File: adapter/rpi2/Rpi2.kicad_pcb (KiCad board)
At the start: 2 copper layers, 56.5 x 65.4 mm, 4 parts

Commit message: routing all traces on pcb
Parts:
- moved Display1 13.7 mm to (150.4, 126.4)
- moved Display2 13.7 mm to (136.4, 126.4)
- moved RPi2 13.2 mm to (105.0, 157.0)
- moved SNES1 8.50 mm to (150.4, 144.7)
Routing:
- net /OE: track 0.00 -> 128.1 mm
- net CLK: track 0.00 -> 127.2 mm
- net STB: track 0.00 -> 125.8 mm
- net SNES_LATCH: track 0.00 -> 105.2 mm
- net SNES_CLK: track 0.00 -> 102.8 mm
- net C: track 0.00 -> 84.2 mm
- net 3V3: track 0.00 -> 82.7 mm
- net A: track 0.00 -> 81.1 mm
- net D: track 0.00 -> 72.6 mm
- net B: track 0.00 -> 70.6 mm, vias 0 -> 2
- net [1]B0: track 0.00 -> 65.8 mm
- net [1]R1: track 0.00 -> 62.4 mm
- net [1]R0: track 0.00 -> 57.7 mm
- net [1]B1: track 0.00 -> 53.3 mm
- net [1]G0: track 0.00 -> 50.5 mm
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- added copper zone on F.Cu, net GND
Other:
- board size 56.5 x 65.4 mm -> 56 x 65 mm
- net class Default: clearance 0.2 -> 0.1; trace_width 0.25 -> 0.2
- net class power added: clearance 0.1, trace_width 0.25, via_dia 0.6, via_drill 0.4
- rule trace_clearance: 0.2 -> 0.1
- rule trace_min: 0.2 -> 0.1

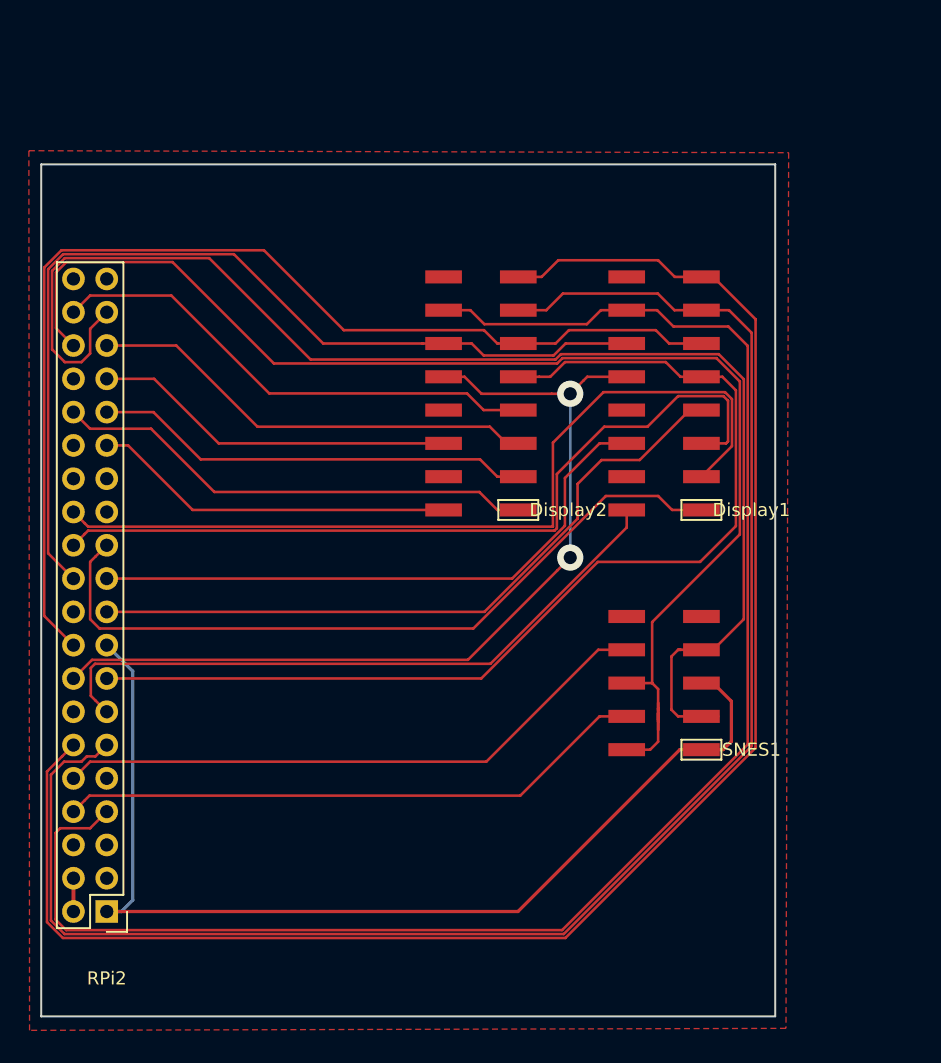
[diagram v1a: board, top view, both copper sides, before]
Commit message: adding PCF8574, finished routing, drill holes unsuitable
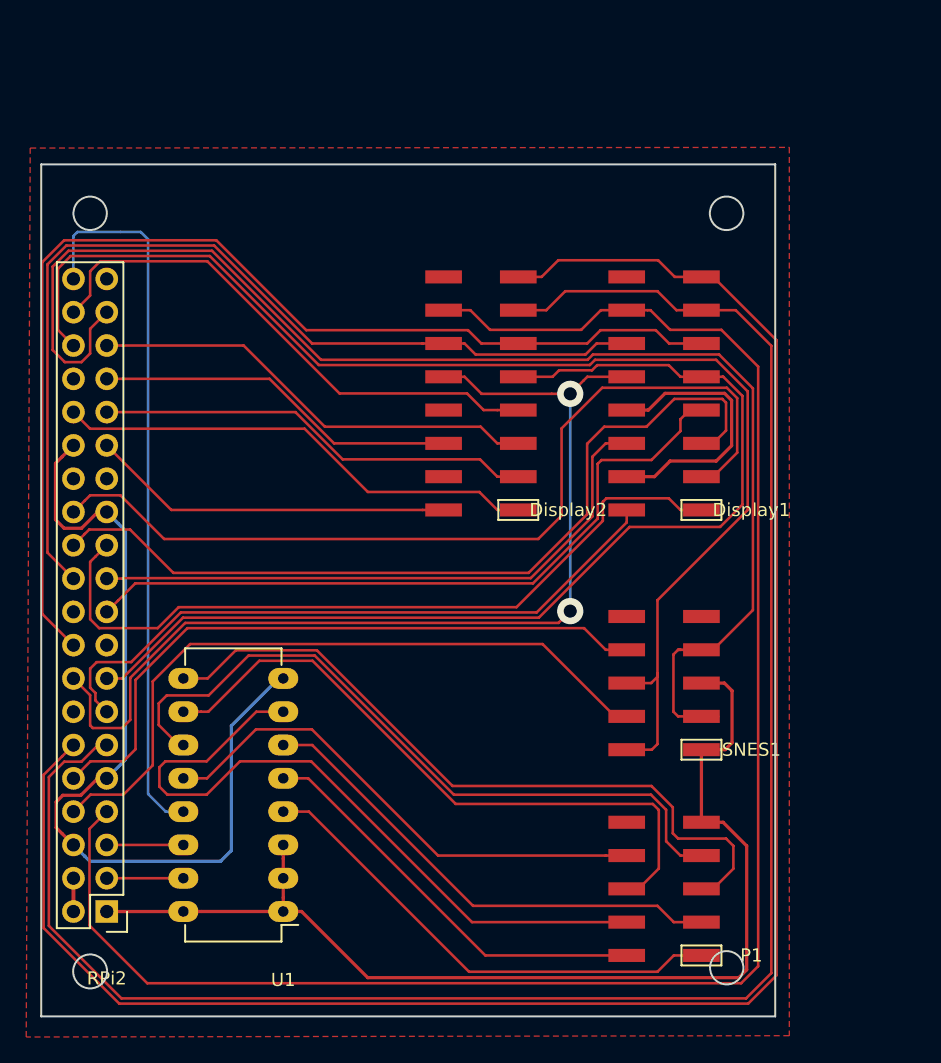
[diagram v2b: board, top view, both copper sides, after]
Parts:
- added P1: CONN_02X05, Pin_Headers_SMD:Pin_Header_SMD_02x05, F.Cu at (150.4, 160.4)
- added U1: PCF8574, Housings_DIP:DIP-16_W7.62mm_LongPads, F.Cu at (118.5, 157.0)
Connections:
- RPi2 pad 14: GND -> Net-(RPi2-Pad14)
- RPi2 pad 17: 3V3 -> Net-(RPi2-Pad17)
- RPi2 pad 20: GND -> Net-(RPi2-Pad20)
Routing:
- net GND: track 0.22 -> 90.2 mm
- net Net-(P1-Pad5): track 0.00 -> 55.0 mm
- net Net-(RPi2-Pad40): track 0.00 -> 54.9 mm
- net Net-(P1-Pad7): track 0.00 -> 54.8 mm
- net Net-(P1-Pad4): track 0.00 -> 54.7 mm
- net Net-(P1-Pad6): track 0.00 -> 50.2 mm
- net Net-(P1-Pad8): track 0.00 -> 39.4 mm
- net Net-(P1-Pad3): track 0.00 -> 37.5 mm
- net Net-(P1-Pad1): track 0.00 -> 37.5 mm
- net Net-(P1-Pad2): track 0.00 -> 31.8 mm
- net CLK: track 127.2 -> 144.5 mm
- net /OE: track 128.1 -> 145.3 mm
- net STB: track 125.8 -> 135.4 mm
- net B: track 70.6 -> 79.4 mm
- net SNES_DATA0: track 45.2 -> 53.5 mm
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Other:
- outline, holes or cut-outs redrawn
- net class Default: clearance 0.1 -> 0.2
- net class power: clearance 0.1 -> 0.2
- rule trace_clearance: 0.1 -> 0.2

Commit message: finalized board
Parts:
- added REF**: Symbol_OSHW-Logo_CopperTop, Symbols:Symbol_OSHW-Logo_CopperTop, F.Cu at (143.8, 155.7)
- moved P1 17.6 mm to (136.4, 149.7)
- moved U1 0.91 mm to (119.4, 157.0)
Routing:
- net Net-(P1-Pad6): track 50.2 -> 26.4 mm
- net Net-(P1-Pad2): track 31.8 -> 12.5 mm
- net Net-(P1-Pad3): track 37.5 -> 18.2 mm
- net Net-(P1-Pad5): track 55.0 -> 35.7 mm
- net Net-(P1-Pad4): track 54.7 -> 35.6 mm
- net Net-(P1-Pad1): track 37.5 -> 18.4 mm
- net Net-(P1-Pad7): track 54.8 -> 35.9 mm
- net Net-(P1-Pad8): track 39.4 -> 20.9 mm
- net 3V3: track 84.5 -> 96.3 mm
- net GND: track 90.2 -> 99.5 mm, vias 0 -> 1
- net STB: track 135.4 -> 132.3 mm
- net CLK: track 144.5 -> 147.3 mm
- net /OE: track 145.3 -> 148.0 mm
- net Net-(RPi2-Pad40): track 54.9 -> 53.3 mm, vias 0 -> 1
- net SNES_DATA1: track 50.7 -> 52.1 mm
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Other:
- board size 56 x 65 mm -> 56.8 x 65 mm

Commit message: changed part names
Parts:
- removed P1: CONN_02X05, Pin_Headers_SMD:Pin_Header_SMD_02x05
- added Expander1: CONN_02X05, Pin_Headers_SMD:Pin_Header_SMD_02x05, F.Cu at (136.4, 149.7)
- ?: renamed from REF**; value Symbol_OSHW-Logo_CopperTop -> (none)
- renumbered SNES1 to SNES1+2
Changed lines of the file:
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@@
     (links 66)
     (no_connects 0)
-    (area 98.8568 98.7044 157.619667 166.573201)
+    (area 99.674999 99.924999 156.575001 165.075001)
     (thickness 1.6)
     (drawings 8)
-    (tracks 420)
+    (tracks 419)
     (zones 0)
     (modules 7)
@@
     (descr "16-lead dip package, row spacing 7.62 mm (300 mils), longer pads")
     (tags "dil dip 2.54 300")
-    (fp_text reference U1 (at 0 -5.22 180) (layer F.SilkS)
-      (effects (font (size 1 1) (thickness 0.15)))
-    )
-    (fp_text value PCF8574 (at 0 -3.72 180) (layer F.Fab)
+    (fp_text reference U1 (at 3.7592 -3.937 180) (layer F.SilkS)
+      (effects (font (size 1 1) (thickness 0.15)))
+    )
+    (fp_text value PCF8574 (at 3.7592 21.3106 180) (layer F.Fab)
       (effects (font (size 1 1) (thickness 0.15)))
     )
@@
     )
   )
-  (module Pin_Headers_SMD:Pin_Header_SMD_02x05 (layer F.Cu)
-    (at 136.4084 149.6822 180)
-    (fp_text reference P1 (at -3.81 0 180) (layer F.SilkS)
-      (effects (font (size 1 1) (thickness 0.15)))
-    )
-    (fp_text value CONN_02X05 (at 0 -2.032 180) (layer F.Fab)
-      (effects (font (size 1 1) (thickness 0.15)))
-    )
-    (fp_line (start -1.524 -0.762) (end 1.524 -0.762) (layer F.SilkS) (width 0.15))
-    (fp_line (start 1.524 -0.762) (end 1.524 0.762) (layer F.SilkS) (width 0.15))
-    (fp_line (start 1.524 0.762) (end -1.524 0.762) (layer F.SilkS) (width 0.15))
-    (fp_line (start -1.524 0.762) (end -1.524 -0.762) (layer F.SilkS) (width 0.15))
-    (pad 1 smd rect (at 0 0 180) (size 2.8 1) (layers F.Cu F.Paste F.Mask)
-      (net 32 "Net-(P1-Pad1)"))
-    (pad 2 smd rect (at 5.7 0 180) (size 2.8 1) (layers F.Cu F.Paste F.Mask)
-      (net 33 "Net-(P1-Pad2)"))
-    (pad 3 smd rect (at 0 2.54 180) (size 2.8 1) (layers F.Cu F.Paste F.Mask)
-      (net 34 "Net-(P1-Pad3)"))
-    (pad 4 smd rect (at 5.7 2.54 180) (size 2.8 1) (layers F.Cu F.Paste F.Mask)
-      (net 35 "Net-(P1-Pad4)"))
-    (pad 5 smd rect (at 0 5.08 180) (size 2.8 1) (layers F.Cu F.Paste F.Mask)
-      (net 36 "Net-(P1-Pad5)"))
-    (pad 6 smd rect (at 5.7 5.08 180) (size 2.8 1) (layers F.Cu F.Paste F.Mask)
-      (net 37 "Net-(P1-Pad6)"))
-    (pad 7 smd rect (at 0 7.62 180) (size 2.8 1) (layers F.Cu F.Paste F.Mask)
-      (net 38 "Net-(P1-Pad7)"))
-    (pad 8 smd rect (at 5.7 7.62 180) (size 2.8 1) (layers F.Cu F.Paste F.Mask)
-      (net 39 "Net-(P1-Pad8)"))
-    (pad 9 smd rect (at 0 10.16 180) (size 2.8 1) (layers F.Cu F.Paste F.Mask)
-      (net 21 3V3))
-    (pad 10 smd rect (at 5.7 10.16 180) (size 2.8 1) (layers F.Cu F.Paste F.Mask)
-      (net 4 GND))
-  )
   (module Pin_Headers:Pin_Header_Straight_2x20 (layer F.Cu)
     (at 105 157 180)
     (descr "Through hole pin header")
     (tags "pin header")
-    (fp_text reference RPi2 (at 0 -5.1 180) (layer F.SilkS)
-      (effects (font (size 1 1) (thickness 0.15)))
-    )
-    (fp_text value CONN_02X20 (at 0 -3.1 180) (layer F.Fab)
+    (fp_text reference RPi2 (at 1.2664 -2.6136 180) (layer F.SilkS)
+      (effects (font (size 1 1) (thickness 0.15)))
+    )
+    (fp_text value CONN_02X20 (at -2.7976 44.7828 450) (layer F.Fab)
       (effects (font (size 1 1) (thickness 0.15)))
     )
@@
   (module Pin_Headers_SMD:Pin_Header_SMD_02x08 (layer F.Cu)
     (at 136.398 126.365 180)
-    (fp_text reference Display2 (at -3.81 0 180) (layer F.SilkS)
-      (effects (font (size 1 1) (thickness 0.15)))
-    )
-    (fp_text value CONN_02X08 (at 0 -2.032 180) (layer F.Fab)
+    (fp_text reference Display2 (at 3.0988 -2.0574 180) (layer F.SilkS)
+      (effects (font (size 1 1) (thickness 0.15)))
+    )
+    (fp_text value CONN_02X08 (at 2.7432 20.0406 180) (layer F.Fab)
       (effects (font (size 1 1) (thickness 0.15)))
     )
@@
   (module Pin_Headers_SMD:Pin_Header_SMD_02x05 (layer F.Cu)
     (at 150.368 144.653 180)
-    (fp_text reference SNES1 (at -3.81 0 180) (layer F.SilkS)
-      (effects (font (size 1 1) (thickness 0.15)))
-    )
-    (fp_text value CONN_02X05 (at 0 -2.032 180) (layer F.Fab)
+    (fp_text reference SNES1+2 (at 2.6924 -2.2606 180) (layer F.SilkS)
+      (effects (font (size 1 1) (thickness 0.15)))
+    )
+    (fp_text value CONN_02X05 (at 2.8448 12.4206 180) (layer F.Fab)
       (effects (font (size 1 1) (thickness 0.15)))
     )
@@
   (module Pin_Headers_SMD:Pin_Header_SMD_02x08 (layer F.Cu)
     (at 150.368 126.365 180)
-    (fp_text reference Display1 (at -3.81 0 180) (layer F.SilkS)
-      (effects (font (size 1 1) (thickness 0.15)))
-    )
-    (fp_text value CONN_02X08 (at 0 -2.032 180) (layer F.Fab)
+    (fp_text reference Display1 (at 2.794 -2.3622 180) (layer F.SilkS)
+      (effects (font (size 1 1) (thickness 0.15)))
+    )
+    (fp_text value CONN_02X08 (at 3.0988 19.9898 180) (layer F.Fab)
       (effects (font (size 1 1) (thickness 0.15)))
     )
@@
     (descr "Symbol, OSHW-Logo, Copper Top,")
     (tags "Symbol, OSHW-Logo, Copper Top,")
-    (fp_text reference REF** (at 0.09906 -4.38912) (layer F.SilkS)
-      (effects (font (size 1 1) (thickness 0.15)))
-    )
-    (fp_text value Symbol_OSHW-Logo_CopperTop (at 0.30988 6.56082) (layer F.Fab)
+    (fp_text reference "" (at 0.09906 -4.38912) (layer F.SilkS)
+      (effects (font (size 1 1) (thickness 0.15)))
+    )
+    (fp_text value "" (at -3.2512 1.6256) (layer F.Fab)
       (effects (font (size 1 1) (thickness 0.15)))
     )
@@
     (fp_line (start 0.35052 0.89916) (end 0.7493 1.89992) (layer F.Cu) (width 0.381))
   )
+  (module Pin_Headers_SMD:Pin_Header_SMD_02x05 (layer F.Cu)
+    (at 136.4084 149.6822 180)
+    (fp_text reference Expander1 (at 3.0584 -2.667 180) (layer F.SilkS)
+      (effects (font (size 1 1) (thickness 0.15)))
+    )
+    (fp_text value CONN_02X05 (at 3.0584 12.3698 180) (layer F.Fab)
+      (effects (font (size 1 1) (thickness 0.15)))
+    )
+    (fp_line (start -1.524 -0.762) (end 1.524 -0.762) (layer F.SilkS) (width 0.15))
+    (fp_line (start 1.524 -0.762) (end 1.524 0.762) (layer F.SilkS) (width 0.15))
+    (fp_line (start 1.524 0.762) (end -1.524 0.762) (layer F.SilkS) (width 0.15))
+    (fp_line (start -1.524 0.762) (end -1.524 -0.762) (layer F.SilkS) (width 0.15))
+    (pad 1 smd rect (at 0 0 180) (size 2.8 1) (layers F.Cu F.Paste F.Mask)
+      (net 32 "Net-(P1-Pad1)"))
+    (pad 2 smd rect (at 5.7 0 180) (size 2.8 1) (layers F.Cu F.Paste F.Mask)
+      (net 33 "Net-(P1-Pad2)"))
+    (pad 3 smd rect (at 0 2.54 180) (size 2.8 1) (layers F.Cu F.Paste F.Mask)
+      (net 34 "Net-(P1-Pad3)"))
+    (pad 4 smd rect (at 5.7 2.54 180) (size 2.8 1) (layers F.Cu F.Paste F.Mask)
+      (net 35 "Net-(P1-Pad4)"))
+    (pad 5 smd rect (at 0 5.08 180) (size 2.8 1) (layers F.Cu F.Paste F.Mask)
+      (net 36 "Net-(P1-Pad5)"))
+    (pad 6 smd rect (at 5.7 5.08 180) (size 2.8 1) (layers F.Cu F.Paste F.Mask)
+      (net 37 "Net-(P1-Pad6)"))
+    (pad 7 smd rect (at 0 7.62 180) (size 2.8 1) (layers F.Cu F.Paste F.Mask)
+      (net 38 "Net-(P1-Pad7)"))
+    (pad 8 smd rect (at 5.7 7.62 180) (size 2.8 1) (layers F.Cu F.Paste F.Mask)
+      (net 39 "Net-(P1-Pad8)"))
+    (pad 9 smd rect (at 0 10.16 180) (size 2.8 1) (layers F.Cu F.Paste F.Mask)
+      (net 21 3V3))
+    (pad 10 smd rect (at 5.7 10.16 180) (size 2.8 1) (layers F.Cu F.Paste F.Mask)
+      (net 4 GND))
+  )
   (gr_circle (center 152.8572 161.8996) (end 154.1272 161.8996) (layer Edge.Cuts) (width 0.15))
   (gr_circle (center 152.8572 103.8352) (end 154.1272 103.8352) (layer Edge.Cuts) (width 0.15))
@@
   (segment (start 106.426 127.946) (end 105.863599 127.383599) (width 0.25) (layer B.Cu) (net 4))
   (segment (start 105.863599 127.383599) (end 105 126.52) (width 0.25) (layer B.Cu) (net 4))
-  (segment (start 118.4656 139.2174) (end 118.1156 139.2174) (width 0.25) (layer B.Cu) (net 4))
   (segment (start 105 146.84) (end 104.3152 146.84) (width 0.25) (layer F.Cu) (net 4))
   (segment (start 104.3152 146.84) (end 103.0224 148.1328) (width 0.25) (layer F.Cu) (net 4))
